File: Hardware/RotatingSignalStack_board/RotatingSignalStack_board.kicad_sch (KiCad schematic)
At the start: 31 parts, among them J1 8P8C_LED_Shielded, J2 Conn_01x05_Pin, SW1 SW_Push, SW2 SW_Push, U1 OKI, U3 Teensy4.1_DEV-16771

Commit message: Redid layout
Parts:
- removed J2: Conn_01x05_Pin, Connector_PinHeader_2.54mm:PinHeader_1x05_P2.54mm_Vertical, symbol Connector:Conn_01x05_Pin
- Conn1: renamed from Conn2; footprint MRDT_Connectors:Square_Anderson_2_H_Side_By_Side -> MRDT_Connectors:Square_Anderson_2_H_Stacked
- Conn2: renamed from Conn3; footprint MRDT_Connectors:Square_Anderson_2_H_Side_By_Side -> MRDT_Connectors:Square_Anderson_2_H_Stacked
- Conn3: renamed from Conn6; footprint MRDT_Connectors:MOLEX_SL_05_Vertical -> MRDT_Connectors:MOLEX_SL_05_Horizontal
- Conn4: renamed from Conn1; footprint MRDT_Connectors:MOLEX_SL_03_Vertical -> MRDT_Connectors:MOLEX_SL_03_Horizontal
- renumbered C3 to C1, C1 to C2, C4 to C3, C5 to C4, C2 to C5, D2 to D1, D1 to D2, D13 to D3, D14 to D4, R2 to R1, R1 to R2, R5 to R3, R3 to R4, R4 to R5, R13 to R6, R18 to R7, U3 to U2
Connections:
- net +12V: now also Conn1.4 (PV+), Conn2.4 (PV+); no longer Conn1.2 (V+Log), Conn2.2 (V+Log)
- net COMP PWR: now also U2.40 (A16); no longer U2.21 (A7)
- net HB_FWD: now also U2.37 (CS3); no longer U2.12 (MISO)
- net HB_RVS: now also U2.36 (CS2); no longer U2.11 (MOSI)
- net I2C SCL: now also U2.16 (A2); no longer U2.19 (A5)
- net I2C SDA: now also U2.17 (A3); no longer U2.18 (A4)
- net JOG A: now also U2.0 (RX1); no longer U2.25 (A11)
- net JOG B: now also U2.1 (TX1); no longer U2.24 (A10)
- net MAG ENABLE: now also U2.18 (A4); no longer U2.15 (A1)
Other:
- note removed: "check the order of these pins for the compass module- make sure not reversed"
- note removed: "pins are here for more mounting options for the compass module"
- note removed: "pretty sure this GND is needed for h bridge"
- moved on the sheet: Conn3

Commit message: Made Rev2 + Gerbs + STEP
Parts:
- removed Conn3: Molex_SL_05, MRDT_Connectors:MOLEX_SL_05_Horizontal, symbol MRDT_Connectors:Molex_SL_05
- removed R3: 0, Resistor_SMD:R_0603_1608Metric_Pad0.98x0.95mm_HandSolder, symbol Device:R
- added Conn3: Molex_SL_04, MRDT_Connectors:MOLEX_SL_04_Horizontal, symbol MRDT_Connectors:Molex_SL_04
- V1, V2, V3, V4: footprint MRDT_Drill_Holes:4_40_Hole_Corner -> MRDT_Drill_Holes:4_40_Hole
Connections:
- net +3.3V: now also R4.2, R5.2, Conn3.1
- net GND: now also Conn3.2
- net HB_FWD: now also Conn4.2; no longer Conn4.1
- net HB_RVS: now also Conn4.1; no longer Conn4.2
- net I2C SCL: now also R4.1, Conn3.3; no longer R5.2
- net I2C SDA: now also R5.1, Conn3.4; no longer R4.2
- net JOG A: now also U2.33 (MCLK2); no longer U2.0 (RX1)
- net JOG B: now also U2.34 (RX8); no longer U2.1 (TX1)
- removed net COMP PWR: R4.1, R5.1, U2.40 (A16)
- net MAG ENABLE: no longer names the net of U2.18 (A4)
- no-connect marks 45 -> 47
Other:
- note added: "Compass"
- note added: "Vin 3vo GND SCL SDA"
- note removed: "3.3v - 0 ohm resistor - solder jumper optional power option for Compass module"
- note removed: "3.3v or the compPwr for i2c, not sure so I will just put compPwr"
- moved on the sheet: R4, R5

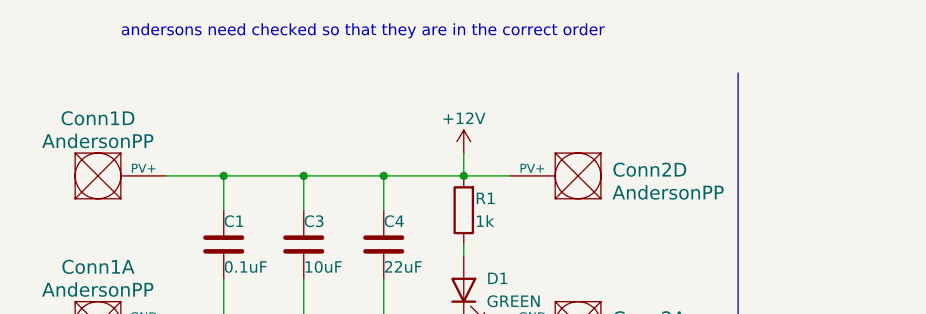
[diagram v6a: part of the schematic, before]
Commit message: Changed 22uF cap + remade Gerbs and STEP
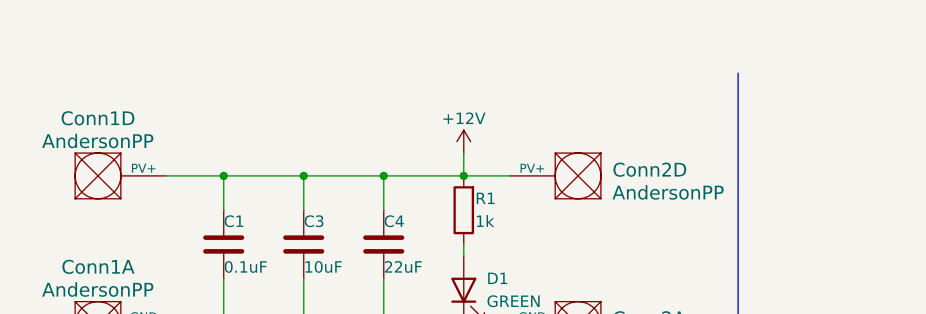
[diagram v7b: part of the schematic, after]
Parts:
- C4: footprint Capacitor_SMD:C_0603_1608Metric_Pad1.08x0.95mm_HandSolder -> Capacitor_THT:CP_Radial_D5.0mm_P2.00mm
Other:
- note removed: "andersons need checked so that they are in the correct order"
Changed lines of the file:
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@@
     (fill (type none))
-  )
-  (text "andersons need checked so that they are in the correct order"
-    (at 22.86 7.62 0)
-    (effects (font (size 1.27 1.27)) (justify left bottom))
   )
   (text "Motor Buttons" (at 153.67 130.81 0)
@@
       (effects (font (size 1.27 1.27)) (justify left))
     )
-    (property "Footprint" "Capacitor_SMD:C_0603_1608Metric_Pad1.08x0.95mm_HandSolder" (at 53.0352 34.29 0)
-      (effects (font (size 1.27 1.27)) hide)
-    )
+    (property "Footprint" "Capacitor_THT:CP_Radial_D5.0mm_P2.00mm" (at 53.0352 34.29 0)
+      (effects (font (size 1.27 1.27)) hide)
+    )
